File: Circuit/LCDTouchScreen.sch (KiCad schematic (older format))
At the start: 0 parts

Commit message: Added footprint for LCD.
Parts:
- added U?: QDTech-3.2in-TFT, symbol QDTech-3.2in-TFT
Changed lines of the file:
@@
 LIBS:bme280
 LIBS:lxdc2xq
+LIBS:qdtech-3.2-tft
 LIBS:IoTuz-cache
 EELAYER 25 0
@@
 $Descr A4 11693 8268
 encoding utf-8
-Sheet 1 7
+Sheet 6 7
 Title ""
 Date ""
@@
 Comment4 ""
 $EndDescr
+$Comp
+L QDTech-3.2in-TFT U?
+U 1 1 5817975D
+P 4200 3000
+F 0 "U?" H 3850 3900 60  0000 C CNN
+F 1 "QDTech-3.2in-TFT" H 4200 2100 60  0000 C CNN
+F 2 "" H 4150 2950 60  0001 C CNN
+F 3 "" H 4150 2950 60  0001 C CNN
+	1    4200 3000
+	1    0    0    -1
+$EndComp
 $EndSCHEMATC

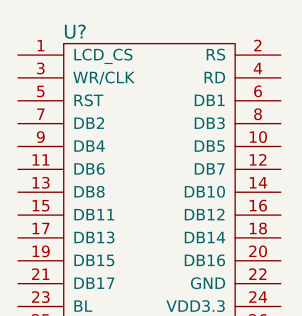
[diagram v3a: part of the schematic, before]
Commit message: Added Alligator clip points.
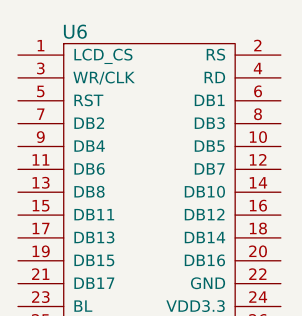
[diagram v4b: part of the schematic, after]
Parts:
- U6: renamed from U?; footprint (none) -> libs:QDTech-3.2in-TFT
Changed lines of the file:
@@
 $EndDescr
 $Comp
-L QDTech-3.2in-TFT U?
+L QDTech-3.2in-TFT U6
 U 1 1 5817975D
 P 4200 3000
-F 0 "U?" H 3850 3900 60  0000 C CNN
+F 0 "U6" H 3850 3900 60  0000 C CNN
 F 1 "QDTech-3.2in-TFT" H 4200 2100 60  0000 C CNN
-F 2 "" H 4150 2950 60  0001 C CNN
+F 2 "libs:QDTech-3.2in-TFT" H 4150 2950 60  0001 C CNN
 F 3 "" H 4150 2950 60  0001 C CNN
 	1    4200 3000

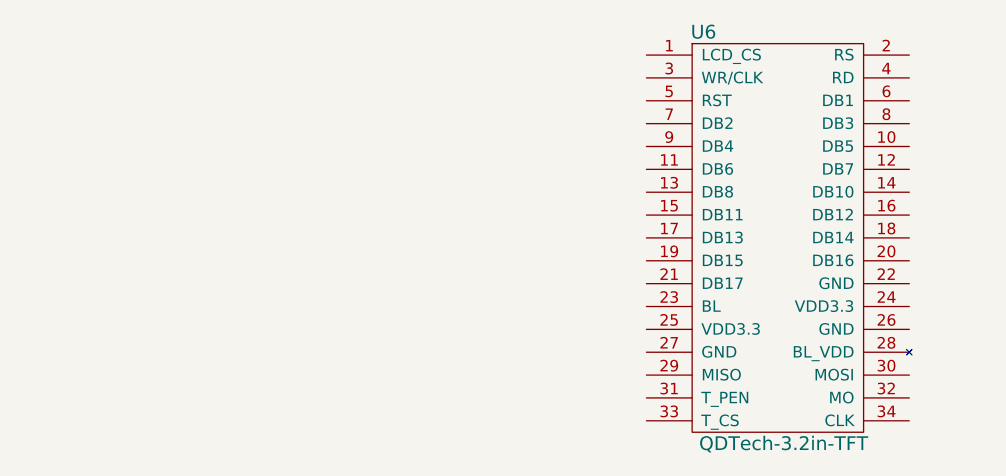
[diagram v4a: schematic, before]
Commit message: Pins to LCD sheet.
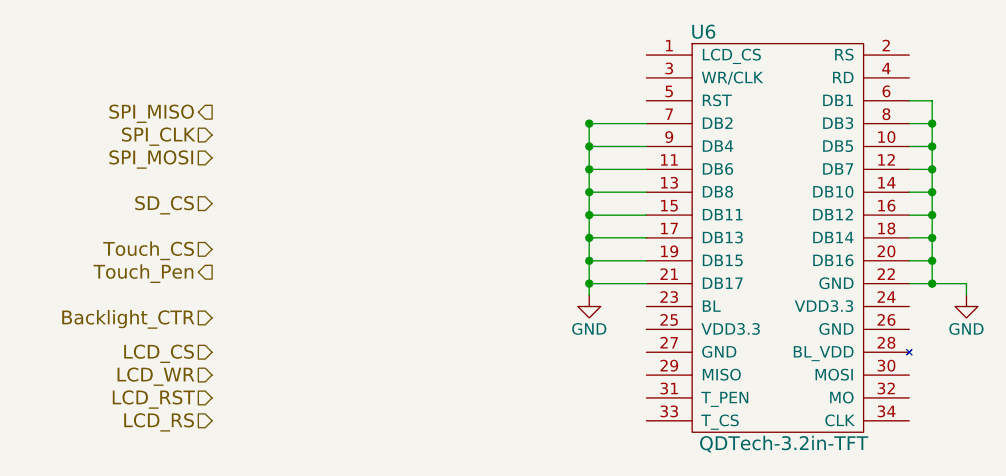
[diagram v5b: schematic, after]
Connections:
- net GND: now reaches U6.10 (DB5)
- net GND: now also U6.11 (DB6), U6.12 (DB7), U6.13 (DB8), U6.14 (DB10), U6.15 (DB11), U6.16 (DB12), U6.17 (DB13), U6.18 (DB14), U6.19 (DB15), U6.20 (DB16), U6.21 (DB17), U6.22 (GND), U6.6 (DB1), U6.7 (DB2), U6.8 (DB3), U6.9 (DB4)
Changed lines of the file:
@@
 	1    0    0    -1
 $EndComp
+Text HLabel 1700 2450 0    60   Output ~ 0
+SPI_MISO
+Text HLabel 1700 2550 0    60   Input ~ 0
+SPI_CLK
+Text HLabel 1700 2650 0    60   Input ~ 0
+SPI_MOSI
+Text HLabel 1700 2850 0    60   Input ~ 0
+SD_CS
+Text HLabel 1700 3050 0    60   Input ~ 0
+Touch_CS
+Text HLabel 1700 3150 0    60   Output ~ 0
+Touch_Pen
+Text HLabel 1700 3350 0    60   Input ~ 0
+Backlight_CTR
+Text HLabel 1700 3500 0    60   Input ~ 0
+LCD_CS
+Text HLabel 1700 3600 0    60   Input ~ 0
+LCD_WR
+Text HLabel 1700 3700 0    60   Input ~ 0
+LCD_RST
+Text HLabel 1700 3800 0    60   Input ~ 0
+LCD_RS
+$Comp
+L GND #PWR?
+U 1 1 581ECEAF
+P 5000 3250
+F 0 "#PWR?" H 5000 3000 50  0001 C CNN
+F 1 "GND" H 5000 3100 50  0000 C CNN
+F 2 "" H 5000 3250 50  0000 C CNN
+F 3 "" H 5000 3250 50  0000 C CNN
+	1    5000 3250
+	1    0    0    -1
+$EndComp
+Wire Wire Line
+	5000 3250 5000 3200
+Wire Wire Line
+	5000 3200 4750 3200
+Wire Wire Line
+	4750 3100 4850 3100
+Wire Wire Line
+	4850 2400 4850 3200
+Connection ~ 4850 3200
+Wire Wire Line
+	4750 2400 4850 2400
+Connection ~ 4850 3100
+Wire Wire Line
+	4750 2500 4850 2500
+Connection ~ 4850 2500
+Connection ~ 4850 2600
+Connection ~ 4850 2700
+Connection ~ 4850 2800
+Connection ~ 4850 2900
+Connection ~ 4850 3000
+Wire Wire Line
+	4750 2600 4850 2600
+Wire Wire Line
+	4750 2700 4850 2700
+Wire Wire Line
+	4750 2800 4850 2800
+Wire Wire Line
+	4750 2900 4850 2900
+Wire Wire Line
+	4750 3000 4850 3000
+$Comp
+L GND #PWR?
+U 1 1 581ECF12
+P 3350 3250
+F 0 "#PWR?" H 3350 3000 50  0001 C CNN
+F 1 "GND" H 3350 3100 50  0000 C CNN
+F 2 "" H 3350 3250 50  0000 C CNN
+F 3 "" H 3350 3250 50  0000 C CNN
+	1    3350 3250
+	1    0    0    -1
+$EndComp
+Wire Wire Line
+	3600 3200 3350 3200
+Connection ~ 3350 3200
+Wire Wire Line
+	3600 2500 3350 2500
+Connection ~ 3350 2500
+Connection ~ 3350 2600
+Connection ~ 3350 2700
+Connection ~ 3350 2800
+Connection ~ 3350 2900
+Connection ~ 3350 3000
+Connection ~ 3350 3100
+Wire Wire Line
+	3600 2600 3350 2600
+Wire Wire Line
+	3600 2700 3350 2700
+Wire Wire Line
+	3600 2800 3350 2800
+Wire Wire Line
+	3600 2900 3350 2900
+Wire Wire Line
+	3600 3000 3350 3000
+Wire Wire Line
+	3600 3100 3350 3100
+Wire Wire Line
+	3350 2500 3350 3250
 $EndSCHEMATC

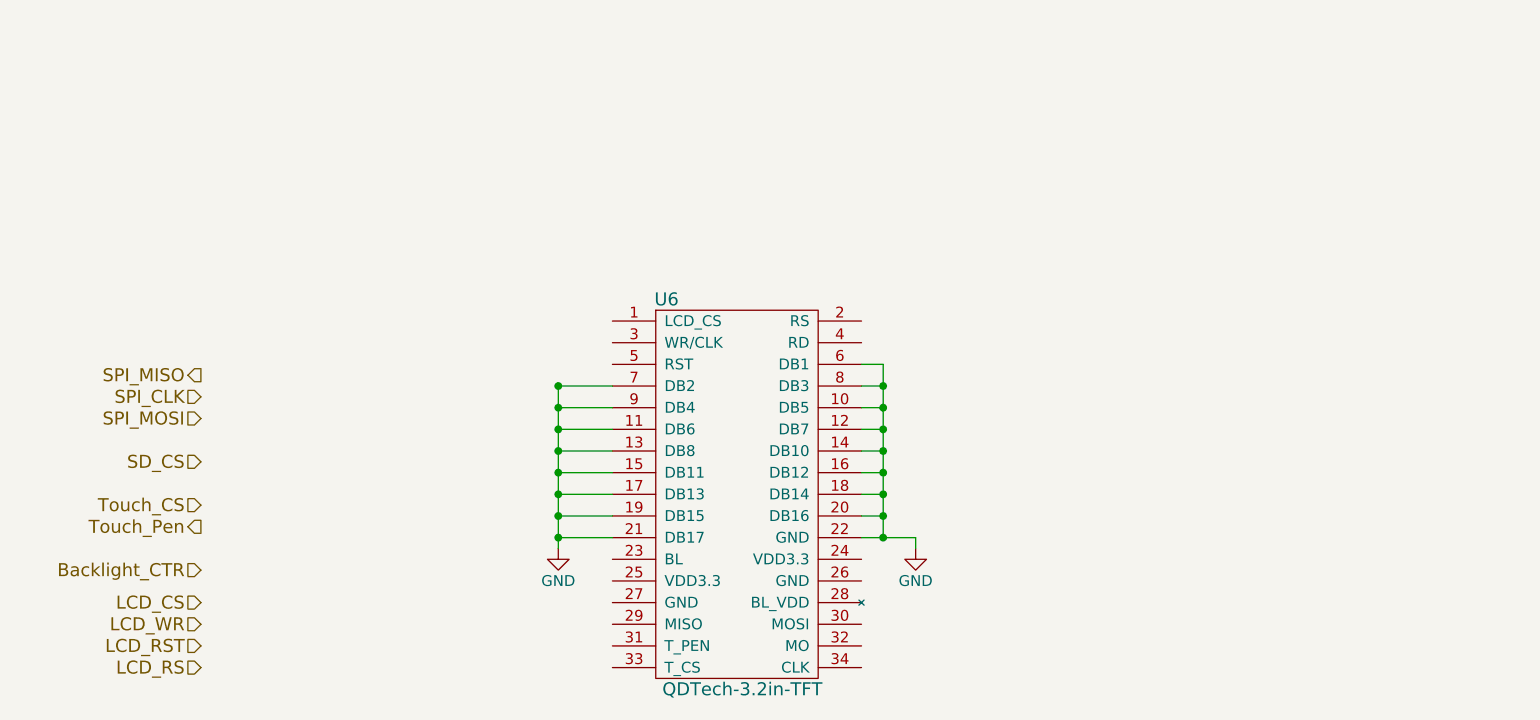
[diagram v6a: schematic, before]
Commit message: Changing touchscreen on schematic.
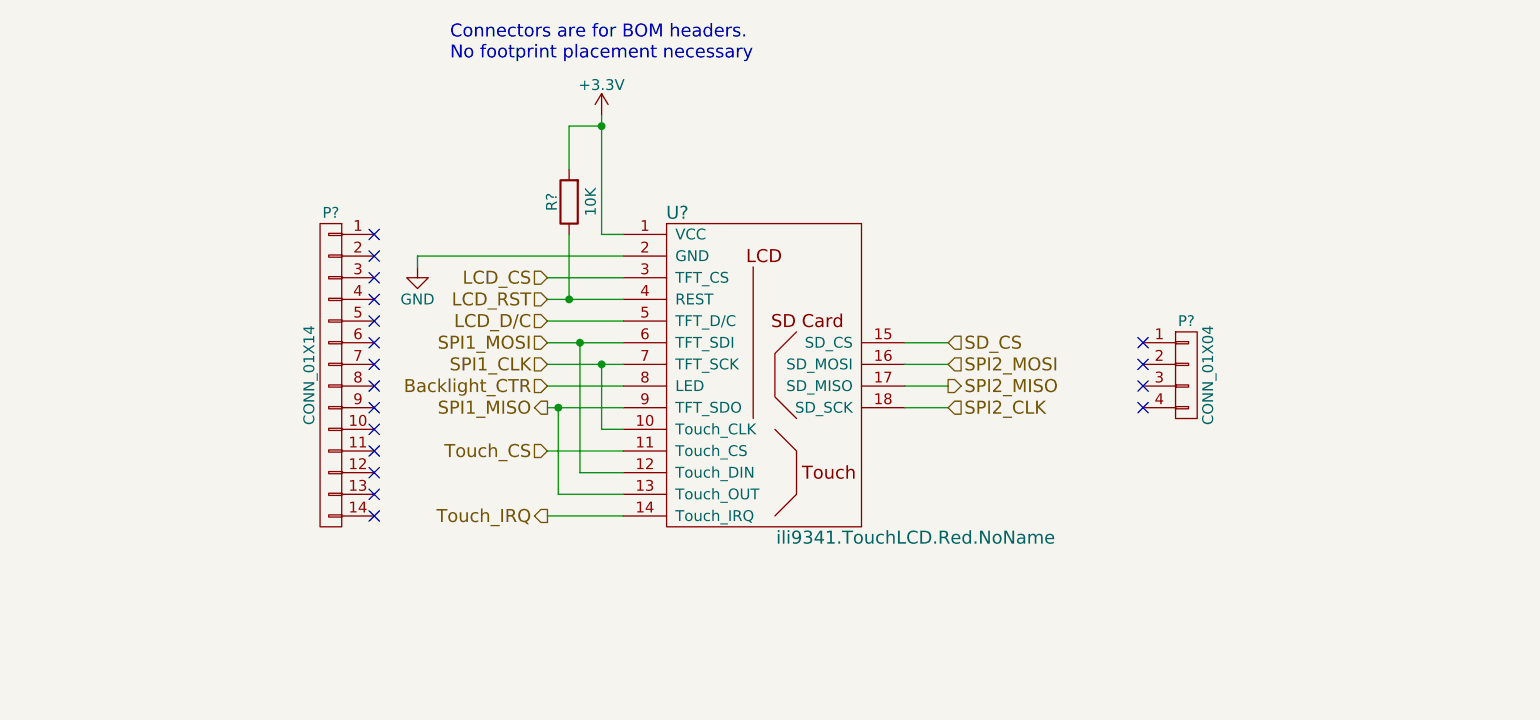
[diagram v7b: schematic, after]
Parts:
- removed U6: QDTech-3.2in-TFT, libs:QDTech-3.2in-TFT, symbol QDTech-3.2in-TFT
- added P?: CONN_01X14, symbol CONN_01X14
- added P?: CONN_01X04, symbol CONN_01X04
- added R?: 10K, Resistors_SMD:R_0603_HandSoldering, symbol R
- added U?: ili9341.TouchLCD.Red.NoName, symbol ili9341.TouchLCD.Red.NoName
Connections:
- net Backlight_CTR: now also U?.8 (LED)
- net GND: now also U?.2 (GND)
- net LCD_CS: now also U?.3 (TFT_CS)
- net LCD_RST: now also R?.1, U?.4 (REST)
- net SD_CS: now also U?.15 (SD_CS)
- net Touch_CS: now also U?.11 (Touch_CS)
- new net +3V3: R?.2, U?.1 (VCC)
- new net LCD_D/C: U?.5 (TFT_D/C)
- new net SPI1_CLK: U?.10 (Touch_CLK), U?.7 (TFT_SCK)
- new net SPI1_MISO: U?.13 (Touch_OUT), U?.9 (TFT_SDO)
- new net SPI1_MOSI: U?.12 (Touch_DIN), U?.6 (TFT_SDI)
- new net SPI2_CLK: U?.18 (SD_SCK)
- new net SPI2_MISO: U?.17 (SD_MISO)
- new net SPI2_MOSI: U?.16 (SD_MOSI)
- new net Touch_IRQ: U?.14 (Touch_IRQ)
- no-connect marks 0 -> 18
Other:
- note added: "Connectors are for BOM headers. \nNo footprint placement necessary"
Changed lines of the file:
@@
 LIBS:nau8814
 LIBS:spu0410hr5h
+LIBS:ili9341.touchlcd.red
 LIBS:IoTuz-cache
 EELAYER 25 0
@@
 Comment4 ""
 $EndDescr
+Text HLabel 3300 2600 0    60   Output ~ 0
+SPI1_MISO
+Text HLabel 3300 2400 0    60   Input ~ 0
+SPI1_CLK
+Text HLabel 3300 2300 0    60   Input ~ 0
+SPI1_MOSI
+Text HLabel 5150 2300 2    60   Input ~ 0
+SD_CS
+Text HLabel 3300 2800 0    60   Input ~ 0
+Touch_CS
+Text HLabel 3300 3100 0    60   Output ~ 0
+Touch_IRQ
+Text HLabel 3300 2500 0    60   Input ~ 0
+Backlight_CTR
+Text HLabel 3300 2000 0    60   Input ~ 0
+LCD_CS
+Text HLabel 3300 2100 0    60   Input ~ 0
+LCD_RST
+Text HLabel 3300 2200 0    60   Input ~ 0
+LCD_D/C
 $Comp
-L QDTech-3.2in-TFT U6
-U 1 1 5817975D
-P 4200 3000
-F 0 "U6" H 3850 3900 60  0000 C CNN
-F 1 "QDTech-3.2in-TFT" H 4200 2100 60  0000 C CNN
-F 2 "libs:QDTech-3.2in-TFT" H 4150 2950 60  0001 C CNN
-F 3 "" H 4150 2950 60  0001 C CNN
-	1    4200 3000
+L CONN_01X14 P?
+U 1 1 5823DD70
+P 2300 2450
+F 0 "P?" H 2300 3200 50  0000 C CNN
+F 1 "CONN_01X14" V 2400 2450 50  0000 C CNN
+F 2 "" H 2300 2450 50  0000 C CNN
+F 3 "" H 2300 2450 50  0000 C CNN
+	1    2300 2450
+	-1   0    0    -1
+$EndComp
+$Comp
+L CONN_01X04 P?
+U 1 1 5823DDB5
+P 6250 2450
+F 0 "P?" H 6250 2700 50  0000 C CNN
+F 1 "CONN_01X04" V 6350 2450 50  0000 C CNN
+F 2 "" H 6250 2450 50  0000 C CNN
+F 3 "" H 6250 2450 50  0000 C CNN
+	1    6250 2450
 	1    0    0    -1
 $EndComp
-Text HLabel 1700 2450 0    60   Output ~ 0
-SPI_MISO
-Text HLabel 1700 2550 0    60   Input ~ 0
-SPI_CLK
-Text HLabel 1700 2650 0    60   Input ~ 0
-SPI_MOSI
-Text HLabel 1700 2850 0    60   Input ~ 0
-SD_CS
-Text HLabel 1700 3050 0    60   Input ~ 0
-Touch_CS
-Text HLabel 1700 3150 0    60   Output ~ 0
-Touch_Pen
-Text HLabel 1700 3350 0    60   Input ~ 0
-Backlight_CTR
-Text HLabel 1700 3500 0    60   Input ~ 0
-LCD_CS
-Text HLabel 1700 3600 0    60   Input ~ 0
-LCD_WR
-Text HLabel 1700 3700 0    60   Input ~ 0
-LCD_RST
-Text HLabel 1700 3800 0    60   Input ~ 0
-LCD_RS
 $Comp
-L GND #PWR063
-U 1 1 581ECEAF
-P 5000 3250
-F 0 "#PWR063" H 5000 3000 50  0001 C CNN
-F 1 "GND" H 5000 3100 50  0000 C CNN
-F 2 "" H 5000 3250 50  0000 C CNN
-F 3 "" H 5000 3250 50  0000 C CNN
-	1    5000 3250
+L ili9341.TouchLCD.Red.NoName U?
+U 1 1 5823E5D0
+P 4300 2450
+F 0 "U?" H 3900 3200 60  0000 C CNN
+F 1 "ili9341.TouchLCD.Red.NoName" H 5000 1700 60  0000 C CNN
+F 2 "" H 4300 2450 60  0001 C CNN
+F 3 "" H 4300 2450 60  0001 C CNN
+	1    4300 2450
+	1    0    0    -1
+$EndComp
+Text HLabel 5150 2500 2    60   Output ~ 0
+SPI2_MISO
+Text HLabel 5150 2600 2    60   Input ~ 0
+SPI2_CLK
+Text HLabel 5150 2400 2    60   Input ~ 0
+SPI2_MOSI
+Text Notes 2850 1000 0    60   ~ 0
+Connectors are for BOM headers. \nNo footprint placement necessary
+NoConn ~ 2500 1800
+NoConn ~ 2500 1900
+NoConn ~ 2500 2000
+NoConn ~ 2500 2100
+NoConn ~ 2500 2200
+NoConn ~ 2500 2300
+NoConn ~ 2500 2400
+NoConn ~ 2500 2500
+NoConn ~ 2500 2600
+NoConn ~ 2500 2700
+NoConn ~ 2500 2800
+NoConn ~ 2500 2900
+NoConn ~ 2500 3000
+NoConn ~ 2500 3100
+NoConn ~ 6050 2300
+NoConn ~ 6050 2400
+NoConn ~ 6050 2500
+NoConn ~ 6050 2600
+Wire Wire Line
+	3300 2400 3650 2400
+Wire Wire Line
+	3550 2400 3550 2700
+Wire Wire Line
+	3550 2700 3650 2700
+Connection ~ 3550 2400
+Wire Wire Line
+	3300 2300 3650 2300
+Wire Wire Line
+	3450 2300 3450 2900
+Wire Wire Line
+	3450 2900 3650 2900
+Connection ~ 3450 2300
+Wire Wire Line
+	3300 2600 3650 2600
+Wire Wire Line
+	3350 2600 3350 3000
+Wire Wire Line
+	3350 3000 3650 3000
+Connection ~ 3350 2600
+Wire Wire Line
+	3650 2800 3300 2800
+Wire Wire Line
+	3650 3100 3300 3100
+Wire Wire Line
+	3650 2500 3300 2500
+Wire Wire Line
+	3300 2200 3650 2200
+Wire Wire Line
+	3650 2100 3300 2100
+Wire Wire Line
+	3300 2000 3650 2000
+$Comp
+L +3.3V #PWR?
+U 1 1 58242261
+P 3550 1250
+F 0 "#PWR?" H 3550 1100 50  0001 C CNN
+F 1 "+3.3V" H 3550 1390 50  0000 C CNN
+F 2 "" H 3550 1250 50  0000 C CNN
+F 3 "" H 3550 1250 50  0000 C CNN
+	1    3550 1250
+	1    0    0    -1
+$EndComp
+$Comp
+L GND #PWR?
+U 1 1 58242289
+P 2700 1950
+F 0 "#PWR?" H 2700 1700 50  0001 C CNN
+F 1 "GND" H 2700 1800 50  0000 C CNN
+F 2 "" H 2700 1950 50  0000 C CNN
+F 3 "" H 2700 1950 50  0000 C CNN
+	1    2700 1950
 	1    0    0    -1
 $EndComp
 Wire Wire Line
-	5000 3250 5000 3200
+	3650 1900 2700 1900
 Wire Wire Line
-	5000 3200 4750 3200
+	2700 1900 2700 1950
 Wire Wire Line
-	4750 3100 4850 3100
+	4950 2300 5150 2300
 Wire Wire Line
-	4850 2400 4850 3200
-Connection ~ 4850 3200
+	4950 2400 5150 2400
 Wire Wire Line
-	4750 2400 4850 2400
-Connection ~ 4850 3100
+	4950 2500 5150 2500
 Wire Wire Line
-	4750 2500 4850 2500
-Connection ~ 4850 2500
-Connection ~ 4850 2600
-Connection ~ 4850 2700
-Connection ~ 4850 2800
-Connection ~ 4850 2900
-Connection ~ 4850 3000
-Wire Wire Line
-	4750 2600 4850 2600
-Wire Wire Line
-	4750 2700 4850 2700
-Wire Wire Line
-	4750 2800 4850 2800
-Wire Wire Line
-	4750 2900 4850 2900
-Wire Wire Line
-	4750 3000 4850 3000
+	4950 2600 5150 2600
 $Comp
-L GND #PWR064
-U 1 1 581ECF12
-P 3350 3250
-F 0 "#PWR064" H 3350 3000 50  0001 C CNN
-F 1 "GND" H 3350 3100 50  0000 C CNN
-F 2 "" H 3350 3250 50  0000 C CNN
-F 3 "" H 3350 3250 50  0000 C CNN
-	1    3350 3250
-	1    0    0    -1
+L R R?
+U 1 1 58247129
+P 3400 1650
+F 0 "R?" V 3480 1650 50  0000 C CNN
+F 1 "10K" V 3300 1650 50  0000 C CNN
+F 2 "Resistors_SMD:R_0603_HandSoldering" V 3330 1650 50  0001 C CNN
+F 3 "" H 3400 1650 50  0000 C CNN
+F 4 "311-10KGRCT-ND" V 3400 1650 60  0001 C CNN "Digikey PN"
+F 5 "http://www.digikey.com.au/product-detail/en/yageo/RC0603JR-0710KL/311-10KGRCT-ND/729647" V 3400 1650 60  0001 C CNN "Link"
+F 6 "RC0603JR-0710KL" V 3400 1650 60  0001 C CNN "Manufacturer PN"
+F 7 "0.10" V 3400 1650 60  0001 C CNN "Unit Cost"
+	1    3400 1650
+	-1   0    0    1
 $EndComp
 Wire Wire Line
-	3600 3200 3350 3200
-Connection ~ 3350 3200
+	3550 1250 3550 1800
 Wire Wire Line
-	3600 2500 3350 2500
-Connection ~ 3350 2500
-Connection ~ 3350 2600
-Connection ~ 3350 2700
-Connection ~ 3350 2800
-Connection ~ 3350 2900
-Connection ~ 3350 3000
-Connection ~ 3350 3100
+	3550 1800 3650 1800
 Wire Wire Line
-	3600 2600 3350 2600
+	3400 1800 3400 2100
+Connection ~ 3400 2100
 Wire Wire Line
-	3600 2700 3350 2700
+	3400 1500 3400 1300
 Wire Wire Line
-	3600 2800 3350 2800
-Wire Wire Line
-	3600 2900 3350 2900
-Wire Wire Line
-	3600 3000 3350 3000
-Wire Wire Line
-	3600 3100 3350 3100
-Wire Wire Line
-	3350 2500 3350 3250
+	3400 1300 3550 1300
+Connection ~ 3550 1300
 $EndSCHEMATC

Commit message: Change to 3v3 regulator.
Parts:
- U6: renamed from U?; footprint (none) -> libs:lcdtouchscreen.2.8inch-red.no-name.ili9341-xpt2046
- gave numbers to parts that had none: 3
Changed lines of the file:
@@
 LIBS:spu0410hr5h
 LIBS:ili9341.touchlcd.red
+LIBS:NCP5501
 LIBS:IoTuz-cache
 EELAYER 25 0
@@
 LCD_D/C
 $Comp
-L CONN_01X14 P?
+L CONN_01X14 P6
 U 1 1 5823DD70
 P 2300 2450
-F 0 "P?" H 2300 3200 50  0000 C CNN
+F 0 "P6" H 2300 3200 50  0000 C CNN
 F 1 "CONN_01X14" V 2400 2450 50  0000 C CNN
 F 2 "" H 2300 2450 50  0000 C CNN
@@
 $EndComp
 $Comp
-L CONN_01X04 P?
+L CONN_01X04 P7
 U 1 1 5823DDB5
 P 6250 2450
-F 0 "P?" H 6250 2700 50  0000 C CNN
+F 0 "P7" H 6250 2700 50  0000 C CNN
 F 1 "CONN_01X04" V 6350 2450 50  0000 C CNN
 F 2 "" H 6250 2450 50  0000 C CNN
@@
 $EndComp
 $Comp
-L ili9341.TouchLCD.Red.NoName U?
+L ili9341.TouchLCD.Red.NoName U6
 U 1 1 5823E5D0
 P 4300 2450
-F 0 "U?" H 3900 3200 60  0000 C CNN
+F 0 "U6" H 3900 3200 60  0000 C CNN
 F 1 "ili9341.TouchLCD.Red.NoName" H 5000 1700 60  0000 C CNN
-F 2 "" H 4300 2450 60  0001 C CNN
+F 2 "libs:lcdtouchscreen.2.8inch-red.no-name.ili9341-xpt2046" H 4300 2450 60  0001 C CNN
 F 3 "" H 4300 2450 60  0001 C CNN
 	1    4300 2450
@@
 Text HLabel 5150 2400 2    60   Input ~ 0
 SPI2_MOSI
-Text Notes 2850 1000 0    60   ~ 0
+Text Notes 1300 1650 0    60   ~ 0
 Connectors are for BOM headers. \nNo footprint placement necessary
 NoConn ~ 2500 1800
@@
 	3300 2000 3650 2000
 $Comp
-L +3.3V #PWR?
+L +3.3V #PWR063
 U 1 1 58242261
 P 3550 1250
-F 0 "#PWR?" H 3550 1100 50  0001 C CNN
+F 0 "#PWR063" H 3550 1100 50  0001 C CNN
 F 1 "+3.3V" H 3550 1390 50  0000 C CNN
 F 2 "" H 3550 1250 50  0000 C CNN
@@
 $EndComp
 $Comp
-L GND #PWR?
+L GND #PWR064
 U 1 1 58242289
 P 2700 1950
-F 0 "#PWR?" H 2700 1700 50  0001 C CNN
+F 0 "#PWR064" H 2700 1700 50  0001 C CNN
 F 1 "GND" H 2700 1800 50  0000 C CNN
 F 2 "" H 2700 1950 50  0000 C CNN
@@
 	4950 2600 5150 2600
 $Comp
-L R R?
+L R R9
 U 1 1 58247129
 P 3400 1650
-F 0 "R?" V 3480 1650 50  0000 C CNN
+F 0 "R9" V 3480 1650 50  0000 C CNN
 F 1 "10K" V 3300 1650 50  0000 C CNN
 F 2 "Resistors_SMD:R_0603_HandSoldering" V 3330 1650 50  0001 C CNN
@@
 	3400 1300 3550 1300
 Connection ~ 3550 1300
+Text Notes 5950 2050 0    60   ~ 0
+Connectors are for BOM headers. \nNo footprint placement necessary
 $EndSCHEMATC
